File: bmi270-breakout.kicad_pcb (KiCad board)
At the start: 2 copper layers, 13.2 x 18.2 mm, 14 parts, among them CN1 AFC10-S04QCA-00, CN2 AFC10-S04QCA-00, J1 Conn_01x07_Pin, J2 Conn_01x05_Pin, U1 BMI270

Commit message: clean up, correct mistakes
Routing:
- net GND: track 4.61 -> 5.95 mm
- net /SCL: track 27.2 -> 27.0 mm, vias 3 -> 2
- net +3.3V: vias 7 -> 6
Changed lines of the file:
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@@
   (dimension (type aligned) (layer "Cmts.User")
     (pts (xy 145.796 110.744) (xy 145.796 92.583))
-    (height -4.826)
-    (gr_text "18.1610 mm" (at 139.82 101.6635 90) (layer "Cmts.User")
+    (height -2.032)
+    (gr_text "18.1610 mm" (at 142.614 101.6635 90) (layer "Cmts.User")
       (effects (font (size 1 1) (thickness 0.15)))
     )
@@
   (dimension (type aligned) (layer "Cmts.User")
     (pts (xy 145.796 110.744) (xy 159.004 110.744))
-    (height 4.572)
-    (gr_text "13.2080 mm" (at 152.4 114.166) (layer "Cmts.User")
+    (height 2.54)
+    (gr_text "13.2080 mm" (at 152.4 112.134) (layer "Cmts.User")
       (effects (font (size 1 1) (thickness 0.15)))
     )
@@
   (via (at 154.813 98.298) (size 0.61) (drill 0.305) (layers "F.Cu" "B.Cu") (net 1))
   (via (at 151.791547 104.446499) (size 0.61) (drill 0.305) (layers "F.Cu" "B.Cu") (net 1))
-  (via (at 150.241 103.759) (size 0.61) (drill 0.305) (layers "F.Cu" "B.Cu") (net 1))
   (via (at 155.2956 104.0892) (size 0.61) (drill 0.305) (layers "F.Cu" "B.Cu") (net 1))
   (segment (start 154.813 98.298) (end 154.813 99.949) (width 0.25) (layer "B.Cu") (net 1))
@@
   (segment (start 153.662 100.846) (end 153.32 100.846) (width 0.25) (layer "F.Cu") (net 2))
   (segment (start 153.924 100.584) (end 153.924 100.571) (width 0.25) (layer "F.Cu") (net 2))
+  (segment (start 155.166 102.39) (end 155.956 101.6) (width 0.25) (layer "F.Cu") (net 2))
+  (segment (start 155.166 102.616) (end 155.166 102.39) (width 0.25) (layer "F.Cu") (net 2))
   (segment (start 153.924 100.571) (end 154.686 99.809) (width 0.25) (layer "F.Cu") (net 2))
   (via (at 158.496 109.22) (size 0.61) (drill 0.305) (layers "F.Cu" "B.Cu") (free) (net 2))
@@
   (segment (start 150.114 101.092) (end 147.8534 101.092) (width 0.25) (layer "F.Cu") (net 3))
   (segment (start 150.368 101.346) (end 150.114 101.092) (width 0.25) (layer "F.Cu") (net 3))
-  (via (at 149.0991 104.5972) (size 0.61) (drill 0.305) (layers "F.Cu" "B.Cu") (net 3))
   (via (at 150.254324 107.201324) (size 0.61) (drill 0.305) (layers "F.Cu" "B.Cu") (net 3))
   (via (at 152.146 94.615) (size 0.61) (drill 0.305) (layers "F.Cu" "B.Cu") (net 3))
   (segment (start 148.7514 100.194) (end 148.8313 100.1141) (width 0.25) (layer "B.Cu") (net 3))
   (segment (start 152.146 96.7994) (end 148.8313 100.1141) (width 0.25) (layer "B.Cu") (net 3))
-  (segment (start 148.7514 104.2495) (end 148.7514 100.194) (width 0.25) (layer "B.Cu") (net 3))
-  (segment (start 149.0991 104.5972) (end 148.7514 104.2495) (width 0.25) (layer "B.Cu") (net 3))
+  (segment (start 148.7514 104.2495) (end 148.7514 104.14) (width 0.25) (layer "B.Cu") (net 3))
   (segment (start 150.254324 107.201324) (end 150.125369 107.201324) (width 0.25) (layer "B.Cu") (net 3))
   (segment (start 148.9196 106.5016) (end 148.9196 104.394) (width 0.25) (layer "B.Cu") (net 3))
   (segment (start 149.606 107.188) (end 148.9196 106.5016) (width 0.25) (layer "B.Cu") (net 3))
+  (segment (start 148.7514 104.14) (end 148.7514 104.2258) (width 0.25) (layer "B.Cu") (net 3))
   (segment (start 150.112045 107.188) (end 149.606 107.188) (width 0.25) (layer "B.Cu") (net 3))
+  (segment (start 148.7514 104.2258) (end 148.9196 104.394) (width 0.25) (layer "B.Cu") (net 3))
   (segment (start 152.146 94.615) (end 152.146 96.7994) (width 0.25) (layer "B.Cu") (net 3))
+  (segment (start 148.7514 104.14) (end 148.7514 100.194) (width 0.25) (layer "B.Cu") (net 3))
   (segment (start 148.8313 100.1141) (end 147.2946 101.6508) (width 0.25) (layer "B.Cu") (net 3))
   (segment (start 150.125369 107.201324) (end 150.112045 107.188) (width 0.25) (layer "B.Cu") (net 3))
@@
   (segment (start 152.045785 103.24787) (end 152.045785 103.531785) (width 0.25) (layer "F.Cu") (net 14))
   (segment (start 152.045785 103.24787) (end 152.045785 103.224215) (width 0.25) (layer "F.Cu") (net 14))
-  (segment (start 152.045785 103.531785) (end 152.15 103.636) (width 0.25) (layer "F.Cu") (net 14))
   (segment (start 152.045785 103.631385) (end 152.5544 104.14) (width 0.25) (layer "F.Cu") (net 14))
   (via (at 152.045785 103.24787) (size 0.61) (drill 0.305) (layers "F.Cu" "B.Cu") (net 14))
@@
   (segment (start 152.052502 103.816499) (end 152.421547 104.185544) (width 0.25) (layer "B.Cu") (net 14))
   (segment (start 152.421547 104.212347) (end 154.9654 106.7562) (width 0.25) (layer "B.Cu") (net 14))
-  (segment (start 153.068556 103.489805) (end 152.65 103.071249) (width 0.25) (layer "F.Cu") (net 15))
-  (segment (start 153.068556 103.489805) (end 153.068556 103.591356) (width 0.25) (layer "F.Cu") (net 15))
-  (segment (start 153.068556 103.591356) (end 153.6172 104.14) (width 0.25) (layer "F.Cu") (net 15))
-  (segment (start 152.65 103.071249) (end 152.65 102.516) (width 0.25) (layer "F.Cu") (net 15))
-  (via (at 153.068556 103.489805) (size 0.61) (drill 0.305) (layers "F.Cu" "B.Cu") (net 15))
-  (segment (start 153.068556 103.489805) (end 154.353751 104.775) (width 0.25) (layer "B.Cu") (net 15))
+  (segment (start 152.853966 103.376766) (end 153.6172 104.14) (width 0.25) (layer "F.Cu") (net 15))
+  (segment (start 152.675785 103.11593) (end 152.675785 102.986915) (width 0.25) (layer "F.Cu") (net 15))
+  (segment (start 152.853966 103.294111) (end 152.853966 103.376766) (width 0.25) (layer "F.Cu") (net 15))
+  (segment (start 152.675785 102.986915) (end 152.65 102.96113) (width 0.25) (layer "F.Cu") (net 15))
+  (segment (start 152.65 102.96113) (end 152.65 102.516) (width 0.25) (layer "F.Cu") (net 15))
+  (segment (start 152.853966 103.294111) (end 152.675785 103.11593) (width 0.25) (layer "F.Cu") (net 15))
+  (via (at 152.853966 103.294111) (size 0.61) (drill 0.305) (layers "F.Cu" "B.Cu") (net 15))
+  (segment (start 154.334855 104.775) (end 156.972 104.775) (width 0.25) (layer "B.Cu") (net 15))
   (segment (start 156.972 104.775) (end 157.5308 104.2162) (width 0.25) (layer "B.Cu") (net 15))
-  (segment (start 154.353751 104.775) (end 156.972 104.775) (width 0.25) (layer "B.Cu") (net 15))
+  (segment (start 152.853966 103.294111) (end 154.334855 104.775) (width 0.25) (layer "B.Cu") (net 15))
   (zone (net 2) (net_name "GND") (layers "F&B.Cu") (hatch edge 0.5)
     (connect_pads (clearance 0.254))

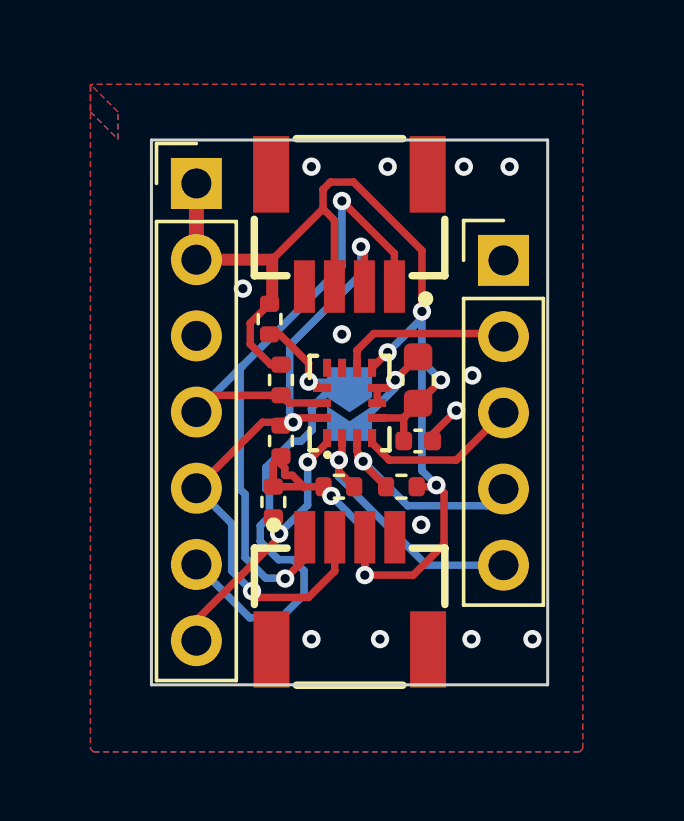
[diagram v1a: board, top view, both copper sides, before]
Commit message: forgot pad labels
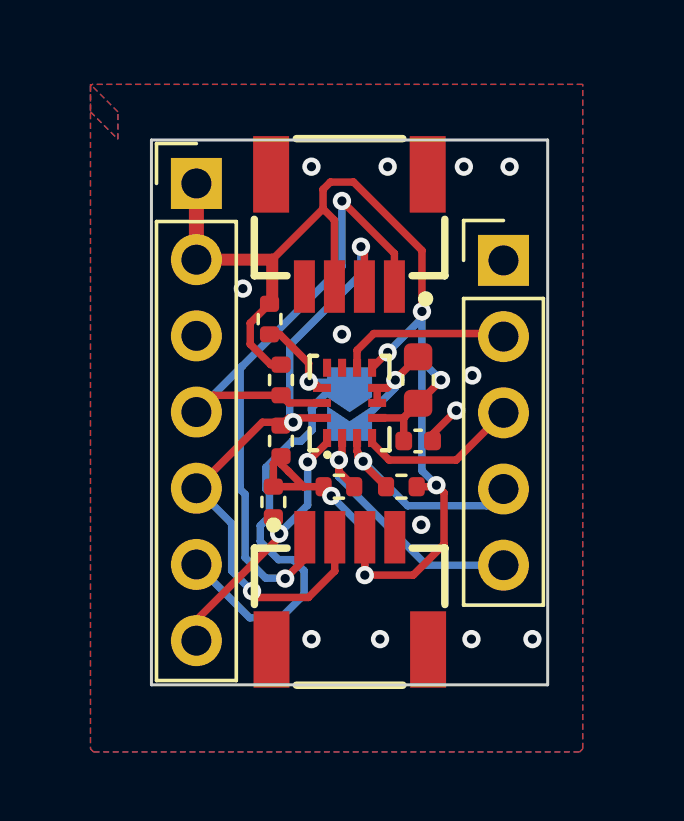
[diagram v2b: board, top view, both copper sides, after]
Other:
- board text added: "3V3"
- board text added: "ADDR"
- board text added: "CSB"
- board text added: "GND"
- board text added: "INT1"
- board text added: "INT2"
- board text added: "SCL"
- board text added: "SDA"
- board text added: "SDO"
- board text added: "XCL"
- board text added: "XDA"
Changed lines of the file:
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@@
   (gr_line (start 145.796 110.744) (end 159.004 110.744)
     (stroke (width 0.1) (type default)) (layer "Edge.Cuts"))
+  (gr_text "GND\n" (at 148.082 99.822) (layer "B.SilkS")
+    (effects (font (size 1 1) (thickness 0.15)) (justify right bottom mirror))
+  )
+  (gr_text "ADDR" (at 152.4 103.378 90) (layer "B.SilkS")
+    (effects (font (size 1 1) (thickness 0.15)) (justify left mirror))
+  )
+  (gr_text "3V3" (at 148.336 97.282) (layer "B.SilkS")
+    (effects (font (size 1 1) (thickness 0.15)) (justify right bottom mirror))
+  )
+  (gr_text "XDA" (at 156.464 107.442) (layer "B.SilkS")
+    (effects (font (size 1 1) (thickness 0.15)) (justify left bottom mirror))
+  )
+  (gr_text "3V3" (at 148.336 94.742) (layer "B.SilkS")
+    (effects (font (size 1 1) (thickness 0.15)) (justify right bottom mirror))
+  )
+  (gr_text "SCL" (at 148.336 102.362) (layer "B.SilkS")
+    (effects (font (size 1 1) (thickness 0.15)) (justify right bottom mirror))
+  )
+  (gr_text "INT2" (at 156.464 99.822) (layer "B.SilkS")
+    (effects (font (size 1 1) (thickness 0.15)) (justify left bottom mirror))
+  )
+  (gr_text "INT1\n" (at 156.464 102.362) (layer "B.SilkS")
+    (effects (font (size 1 1) (thickness 0.15)) (justify left bottom mirror))
+  )
+  (gr_text "SDO" (at 148.336 109.982) (layer "B.SilkS")
+    (effects (font (size 1 1) (thickness 0.15)) (justify right bottom mirror))
+  )
+  (gr_text "XCL" (at 156.464 104.902) (layer "B.SilkS")
+    (effects (font (size 1 1) (thickness 0.15)) (justify left bottom mirror))
+  )
+  (gr_text "CSB" (at 148.336 107.442) (layer "B.SilkS")
+    (effects (font (size 1 1) (thickness 0.15)) (justify right bottom mirror))
+  )
+  (gr_text "SDA" (at 148.336 104.902) (layer "B.SilkS")
+    (effects (font (size 1 1) (thickness 0.15)) (justify right bottom mirror))
+  )
   (dimension (type aligned) (layer "Cmts.User")
     (pts (xy 145.796 110.744) (xy 145.796 92.583))
@@
   (segment (start 149.86 104.138) (end 149.86 103.378) (width 0.25) (layer "F.Cu") (net 1))
   (segment (start 155.2448 104.14) (end 155.2956 104.0892) (width 0.25) (layer "F.Cu") (net 1))
+  (segment (start 150.366 103.632) (end 150.114 103.38) (width 0.25) (layer "F.Cu") (net 1))
   (segment (start 153.67 99.6635) (end 153.6625 99.6635) (width 0.25) (layer "F.Cu") (net 1))
   (segment (start 155.448 100.597) (end 154.686 101.359) (width 0.25) (layer "F.Cu") (net 1))
@@
   (segment (start 152.908 107.0864) (end 154.5226 107.0864) (width 0.25) (layer "F.Cu") (net 1))
   (segment (start 147.2946 94.0308) (end 147.2946 96.5708) (width 0.5) (layer "F.Cu") (net 1))
-  (segment (start 150.241 103.507) (end 150.114 103.38) (width 0.25) (layer "F.Cu") (net 1))
   (segment (start 154.6372 104.14) (end 155.2448 104.14) (width 0.25) (layer "F.Cu") (net 1))
   (segment (start 152.908 107.0864) (end 152.908 105.826) (width 0.25) (layer "F.Cu") (net 1))
   (segment (start 151.516 94.875955) (end 149.821155 96.5708) (width 0.25) (layer "F.Cu") (net 1))
   (segment (start 149.088 99.387538) (end 149.772462 100.072) (width 0.25) (layer "F.Cu") (net 1))
-  (segment (start 150.114 103.38) (end 150.114 103.124) (width 0.25) (layer "F.Cu") (net 1))
   (segment (start 152.908 105.826) (end 152.908 105.108538) (width 0.25) (layer "F.Cu") (net 1))
   (segment (start 154.206 101.839) (end 154.686 101.359) (width 0.25) (layer "F.Cu") (net 1))
-  (segment (start 150.241 103.759) (end 150.241 103.507) (width 0.25) (layer "F.Cu") (net 1))
   (segment (start 151.76 93.985) (end 152.532 93.985) (width 0.25) (layer "F.Cu") (net 1))
   (segment (start 154.813 96.266) (end 154.813 98.298) (width 0.25) (layer "F.Cu") (net 1))
   (segment (start 155.448 100.584) (end 155.448 100.597) (width 0.25) (layer "F.Cu") (net 1))
   (segment (start 155.5496 106.0594) (end 155.5496 104.3432) (width 0.25) (layer "F.Cu") (net 1))
+  (segment (start 150.114 103.38) (end 150.114 103.124) (width 0.25) (layer "F.Cu") (net 1))
   (segment (start 151.5344 104.14) (end 151.5344 104.189352) (width 0.25) (layer "F.Cu") (net 1))
   (segment (start 154.206 102.616) (end 154.206 101.839) (width 0.25) (layer "F.Cu") (net 1))
   (segment (start 151.895 95.254955) (end 151.516 94.875955) (width 0.25) (layer "F.Cu") (net 1))
   (segment (start 153.32 101.846) (end 154.199 101.846) (width 0.25) (layer "F.Cu") (net 1))
-  (segment (start 150.493 103.759) (end 150.241 103.759) (width 0.25) (layer "F.Cu") (net 1))
   (segment (start 149.821155 96.5708) (end 149.821155 97.953845) (width 0.4) (layer "F.Cu") (net 1))
   (segment (start 153.6625 99.6635) (end 153.15 100.176) (width 0.25) (layer "F.Cu") (net 1))
+  (segment (start 150.874 104.14) (end 150.368 103.634) (width 0.25) (layer "F.Cu") (net 1))
   (segment (start 152.532 93.985) (end 154.813 96.266) (width 0.25) (layer "F.Cu") (net 1))
-  (segment (start 150.874 104.14) (end 150.493 103.759) (width 0.25) (layer "F.Cu") (net 1))
+  (segment (start 150.368 103.634) (end 150.368 103.632) (width 0.25) (layer "F.Cu") (net 1))
+  (segment (start 150.368 103.632) (end 150.366 103.632) (width 0.25) (layer "F.Cu") (net 1))
   (via (at 153.67 99.6635) (size 0.61) (drill 0.305) (layers "F.Cu" "B.Cu") (net 1))
   (via (at 155.448 100.584) (size 0.61) (drill 0.305) (layers "F.Cu" "B.Cu") (net 1))

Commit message: documentation, migrate to kicad 8, fix address jumper, add branding
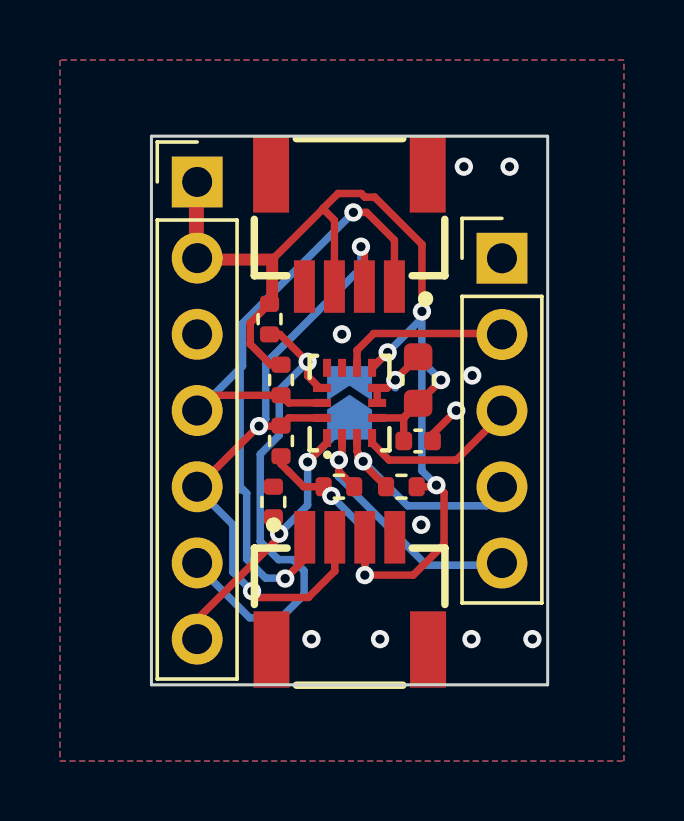
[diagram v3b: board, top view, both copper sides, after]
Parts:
- moved J2 0.09 mm to (157.5, 96.5)
- moved J1 0.06 mm to (147.3, 94.0)
- turned JP1 to 90 degrees
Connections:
- JP1 pad 1: /CSB -> /SDO
- JP1 pad 2: GND -> +3.3V
- R4 pad 1: +3.3V -> GND
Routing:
- net GND: track 5.95 -> 3.91 mm, vias 14 -> 11
- net /SDO: track 9.18 -> 11.1 mm
- net /CSB: track 18.6 -> 16.9 mm
- net +3.3V: track 50.7 -> 49.6 mm
- net /SCL: track 27.0 -> 26.5 mm
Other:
- board size 13.2 x 18.2 mm -> 13.2 x 18.3 mm
- board text added: "FTI"

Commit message: fix qwiic pinout, rework footprint
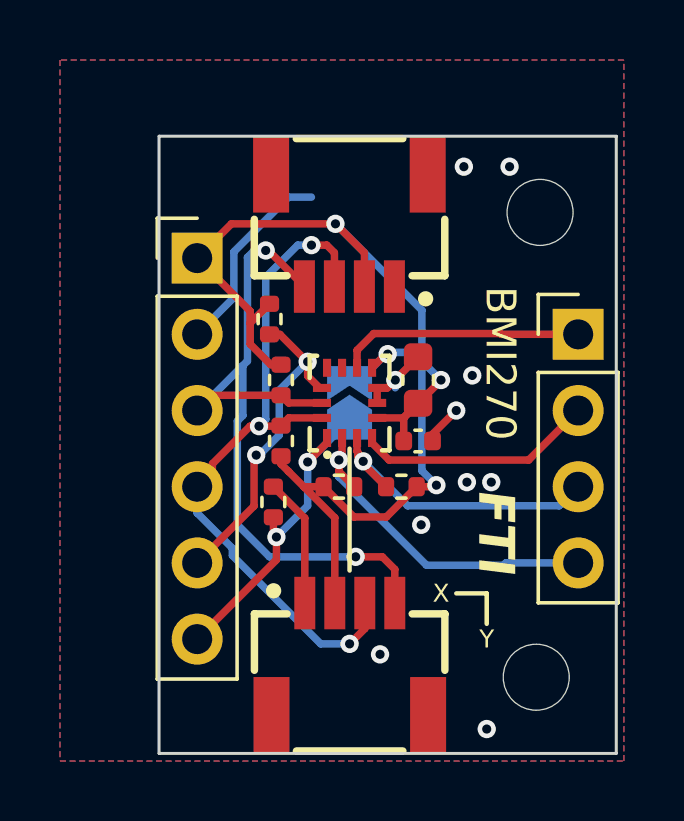
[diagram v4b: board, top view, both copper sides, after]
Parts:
- added H1: MountingHole, MountingHole:MountingHole_2.2mm_M2, F.Cu at (158.8, 95.0)
- added H2: MountingHole, MountingHole:MountingHole_2.2mm_M2, F.Cu at (158.6, 110.5)
- J1: value Conn_01x07_Pin -> Conn_01x06_Pin; footprint Connector_PinHeader_2.54mm:PinHeader_1x07_P2.54mm_Vertical -> Connector_PinHeader_2.54mm:PinHeader_1x06_P2.54mm_Vertical
- J2: value Conn_01x05_Pin -> Conn_01x04_Pin; footprint Connector_PinHeader_2.54mm:PinHeader_1x05_P2.54mm_Vertical -> Connector_PinHeader_2.54mm:PinHeader_1x04_P2.54mm_Vertical
- moved J2 3.59 mm to (160.0, 99.1)
- moved J1 2.54 mm to (147.3, 96.5)
- moved CN2 2.19 mm to (152.4, 109.9)
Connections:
- CN1 pad 1: /SCL -> GND
- CN1 pad 2: /SDA -> +3.3V
- CN1 pad 3: +3.3V -> /SDA
- CN1 pad 4: GND -> /SCL
- CN1 pad 5: unconnected-(CN1-Pad5) -> GND
- CN1 pad 6: unconnected-(CN1-Pad6) -> GND
- CN2 pad 1: /SCL -> GND
- CN2 pad 2: /SDA -> +3.3V
- CN2 pad 3: +3.3V -> /SDA
- CN2 pad 4: GND -> /SCL
- CN2 pad 5: unconnected-(CN2-Pad5) -> GND
- CN2 pad 6: unconnected-(CN2-Pad6) -> GND
- J1 pad 2: +3.3V -> GND
- J1 pad 3: GND -> /SCL
- J1 pad 4: /SCL -> /SDA
- J1 pad 5: /SDA -> /CSB
- J1 pad 6: /CSB -> /SDO
- J2 pad 1: unconnected-(J2-Pin_1-Pad1) -> /INT2
- J2 pad 2: /INT2 -> /INT1
- J2 pad 3: /INT1 -> /XCL
- J2 pad 4: /XCL -> /XDA
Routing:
- net GND: track 3.91 -> 14.8 mm, vias 11 -> 10
- net +3.3V: track 49.6 -> 43.4 mm, vias 6 -> 4
- net /CSB: track 16.9 -> 11.2 mm, vias 1 -> 2
- net /INT1: track 5.43 -> 7.95 mm
- net /XDA: track 9.45 -> 12.0 mm
- net /XCL: track 7.55 -> 10.1 mm
- net /INT2: track 5.74 -> 8.20 mm
- net /SDA: track 22.6 -> 24.6 mm
- net /SCL: track 26.5 -> 25.2 mm
- net /SDO: track 11.1 -> 11.8 mm
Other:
- board size 13.2 x 18.3 mm -> 15.2 x 20.6 mm
- board text added: "BMI270"
- board text added: "X"
- board text added: "Y"

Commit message: allign mounting holes
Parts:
- moved H2 0.13 mm to (158.8, 110.5)
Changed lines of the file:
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@@
 	(footprint "MountingHole:MountingHole_2.2mm_M2"
 		(layer "F.Cu")
-		(at 158.623 110.49)
+		(at 158.75 110.49)
 		(descr "Mounting Hole 2.2mm, no annular, M2")
 		(tags "mounting hole 2.2mm no annular m2")

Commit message: gitignore and pcb
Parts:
- J1, J2: moved to B.Cu
- moved J1 1.27 mm to (146.1, 96.5), turned to 180 degrees
- moved CN1 0.25 mm to (152.4, 95.9)
- moved R6 0.08 mm to (154.1, 104.1)
- turned J2 to 180 degrees
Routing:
- net GND: track 14.8 -> 8.22 mm, vias 10 -> 15
- net /SCL: track 25.2 -> 27.0 mm
- net /CSB: track 11.2 -> 12.5 mm
- net +3.3V: track 43.4 -> 44.3 mm
- net /SDA: track 24.6 -> 25.3 mm
- net /SDO: track 11.8 -> 12.4 mm
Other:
- board size 15.2 x 20.6 mm -> 16.5 x 20.3 mm
- board text added: "G"
- board text added: "V"
